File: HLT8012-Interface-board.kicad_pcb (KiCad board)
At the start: 2 copper layers, 33 x 32.5 mm, 18 parts, among them J1 +(ev), J2 -(ev), J3 LOAD, J4 DC, U1 HLW8012

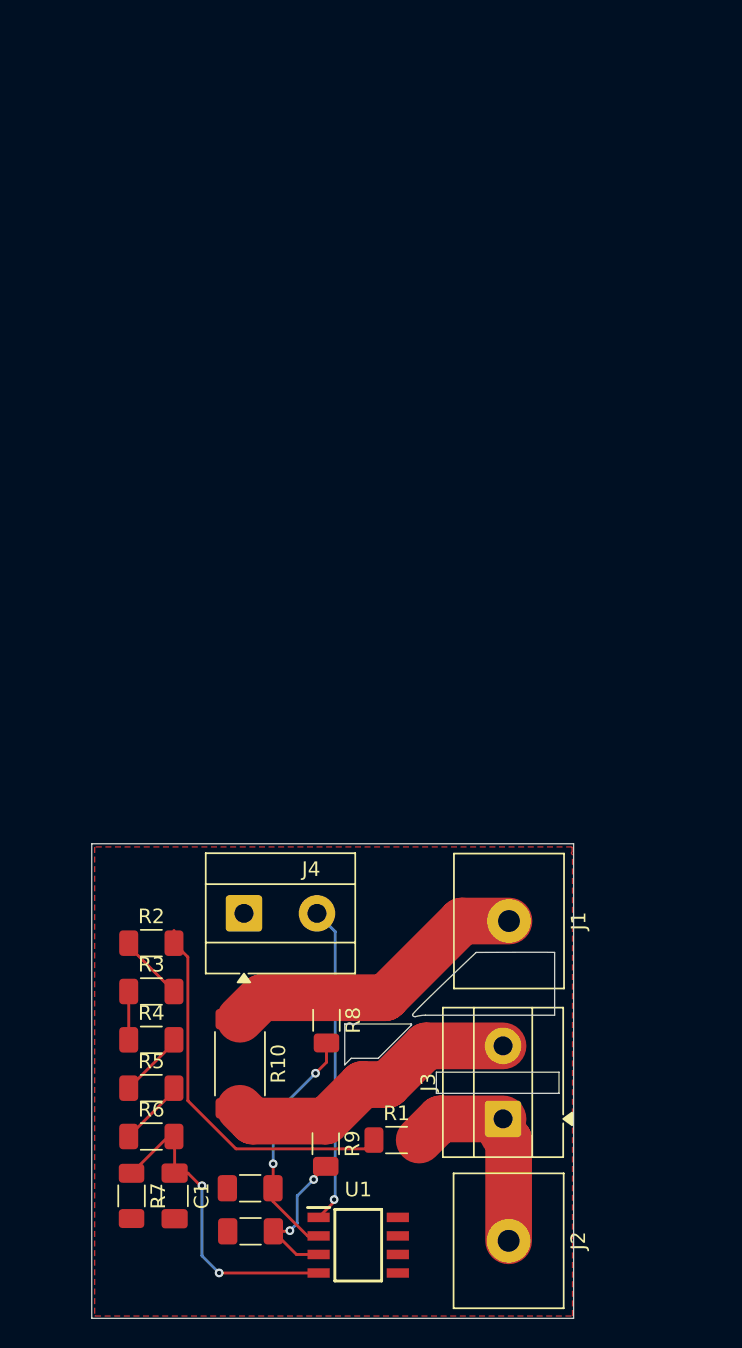
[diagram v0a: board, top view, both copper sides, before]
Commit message: ESP01 fix
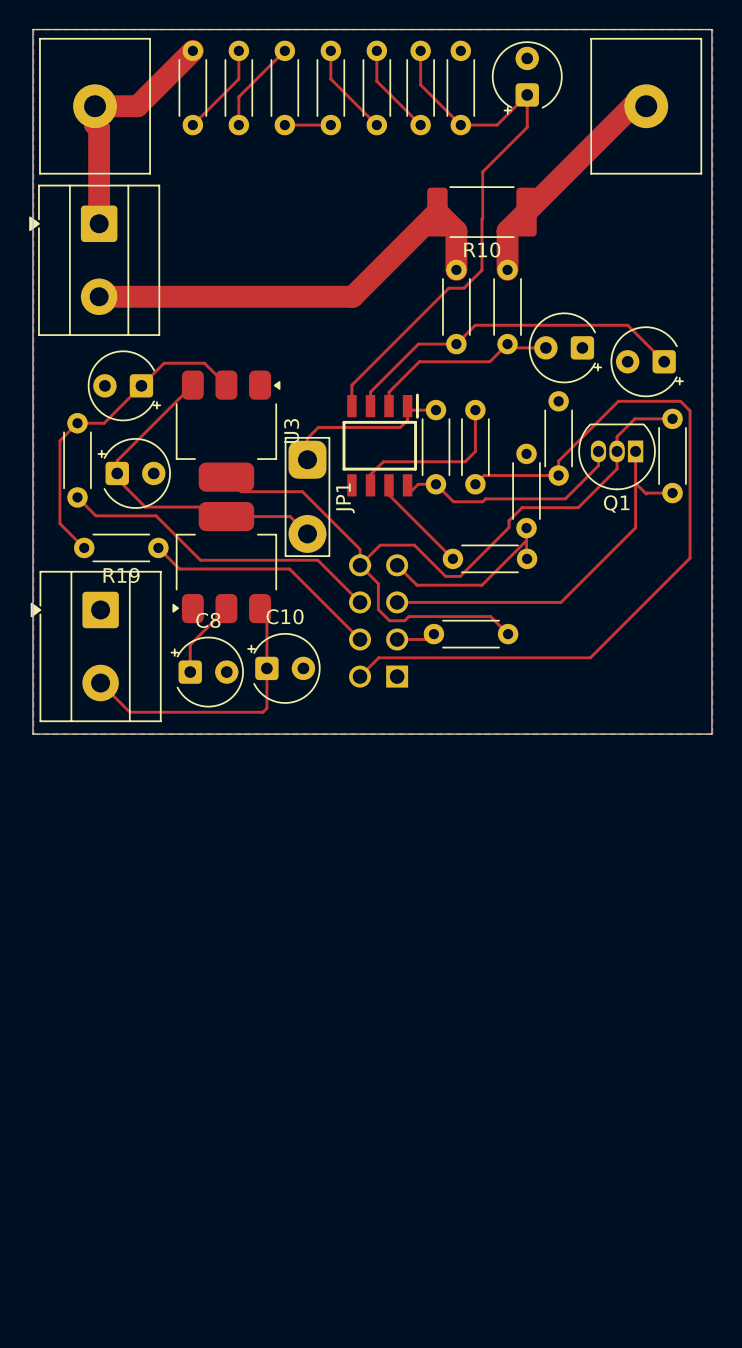
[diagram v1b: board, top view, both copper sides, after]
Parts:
- added C10: 22uF, Capacitor_THT:CP_Radial_Tantal_D4.5mm_P2.50mm, F.Cu at (122.2, 92.8)
- added C4: 22uF, Capacitor_THT:CP_Radial_Tantal_D4.5mm_P2.50mm, F.Cu at (112.0, 79.4)
- added C6: 100uF, Capacitor_THT:CP_Radial_Tantal_D4.5mm_P2.50mm, F.Cu at (113.6, 73.4)
- added C8: 100uF, Capacitor_THT:CP_Radial_Tantal_D4.5mm_P2.50mm, F.Cu at (117.0, 93.0)
- added JP1: Jumper_2_Bridged, TestPoint:TestPoint_2Pads_Pitch5.08mm_Drill1.3mm, F.Cu at (125.0, 78.5)
- added Q1: 2N7000, Package_TO_SOT_THT:TO-92_Inline, F.Cu at (147.5, 77.9)
- added R11: 470K, Resistor_THT:R_Axial_DIN0204_L3.6mm_D1.6mm_P5.08mm_Horizontal, F.Cu at (132.8, 55.5)
- added R12: 10K, Resistor_THT:R_Axial_DIN0204_L3.6mm_D1.6mm_P5.08mm_Horizontal, F.Cu at (133.8, 80.1)
- added R13: 10K, Resistor_THT:R_Axial_DIN0204_L3.6mm_D1.6mm_P5.08mm_Horizontal, F.Cu at (135.0, 85.2)
- added R14: 15K, Resistor_THT:R_Axial_DIN0204_L3.6mm_D1.6mm_P5.08mm_Horizontal, F.Cu at (140.0, 83.1)
- added R15: 15K, Resistor_THT:R_Axial_DIN0204_L3.6mm_D1.6mm_P5.08mm_Horizontal, F.Cu at (142.2, 74.5)
- added R16: 10K, Resistor_THT:R_Axial_DIN0204_L3.6mm_D1.6mm_P5.08mm_Horizontal, F.Cu at (136.5, 80.1)
- added R17: 10K, Resistor_THT:R_Axial_DIN0204_L3.6mm_D1.6mm_P5.08mm_Horizontal, F.Cu at (109.2, 81.0)
- added R18: 10K, Resistor_THT:R_Axial_DIN0204_L3.6mm_D1.6mm_P5.08mm_Horizontal, F.Cu at (138.7, 90.4)
- added R19: 10K, Resistor_THT:R_Axial_DIN0204_L3.6mm_D1.6mm_P5.08mm_Horizontal, F.Cu at (114.8, 84.5)
- added U2: ESP-01, ESP-01:MODULE_ESP-01, B.Cu at (139.5, 89.5)
- added U3: AMS1117-3.3, Package_TO_SOT_SMD:SOT-223-3_TabPin2, F.Cu at (119.5, 76.5)
- added U4: AMS1117-5.0, Package_TO_SOT_SMD:SOT-223-3_TabPin2, F.Cu at (119.5, 85.5)
- C1, C2, C3: footprint Capacitor_SMD:C_1206_3216Metric_Pad1.33x1.80mm_HandSolder -> Capacitor_THT:CP_Radial_Tantal_D4.5mm_P2.50mm
- R1, R2, R3, R4, R5, R8, R9: footprint Resistor_SMD:R_1206_3216Metric_Pad1.30x1.75mm_HandSolder -> Resistor_THT:R_Axial_DIN0204_L3.6mm_D1.6mm_P5.08mm_Horizontal
- R6: value 470K -> 10K; footprint Resistor_SMD:R_1206_3216Metric_Pad1.30x1.75mm_HandSolder -> Resistor_THT:R_Axial_DIN0204_L3.6mm_D1.6mm_P5.08mm_Horizontal
- R7: value 470K -> 1K; footprint Resistor_SMD:R_1206_3216Metric_Pad1.30x1.75mm_HandSolder -> Resistor_THT:R_Axial_DIN0204_L3.6mm_D1.6mm_P5.08mm_Horizontal
- moved J2 82.7 mm to (110.5, 54.2)
- moved C1 79.2 mm to (140.1, 53.5), turned to 90 degrees
- moved R7 76.7 mm to (135.5, 55.5), turned to 90 degrees
- moved R1 70.9 mm to (117.2, 55.5), turned to 90 degrees
- moved R5 67.7 mm to (129.8, 55.5), turned to 90 degrees
- moved J3 67.3 mm to (110.7, 62.3), turned to -90 degrees
- moved C3 65.9 mm to (149.4, 71.8)
- moved R4 63.8 mm to (126.6, 55.5), turned to 90 degrees
- moved C2 61.9 mm to (143.8, 70.8), turned to 180 degrees
- moved R10 60.6 mm to (136.9, 61.5), turned to 180 degrees
- moved R9 60.5 mm to (135.2, 65.5)
- moved R3 60.0 mm to (123.5, 55.5), turned to 90 degrees
- moved R6 56.7 mm to (150.0, 80.7), turned to 90 degrees
- moved J1 56.6 mm to (148.2, 54.2)
- moved R2 56.3 mm to (120.3, 55.5), turned to 90 degrees
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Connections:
- J4 pad 2: +5V -> +12V
- R5 pad 2: Net-(R5-Pad2) -> Net-(R11-Pad1)
- R6 pad 1: Net-(R5-Pad2) -> SEL
- R6 pad 2: V2P -> +3.3V
- U1 pad 1: +5V -> Net-(JP1-A)
- U1 pad 6: CF -> Net-(U1-CF)
- U1 pad 7: CF1 -> Net-(U1-CF1)
- U1 pad 8: SEL -> Net-(Q1-D)
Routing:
- net +3.3V: track 0.00 -> 78.4 mm
- net CF: track 0.00 -> 54.2 mm
- net SEL: track 0.00 -> 26.5 mm
- net Net-(U2-~{RST}): track 0.00 -> 22.3 mm
- net Net-(R1-Pad1): track 26.4 -> 6.38 mm
- net +12V: track 0.00 -> 19.4 mm
- net Net-(U2-CH_PD): track 0.00 -> 16.4 mm
- net V2P: track 22.6 -> 38.5 mm, vias 2 -> 0
- net Net-(Q1-D): track 0.00 -> 15.9 mm
- net Net-(U1-V1N): track 10.5 -> 24.2 mm, vias 2 -> 0
- net CF1: track 0.00 -> 12.8 mm
- net Net-(JP1-A): track 0.00 -> 11.9 mm
- net Net-(U1-CF): track 0.00 -> 11.4 mm
- net /LOAD: track 20.5 -> 30.1 mm
- net +5V: track 21.8 -> 29.2 mm, vias 1 -> 0
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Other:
- board size 33 x 32.5 mm -> 46.5 x 48.2 mm

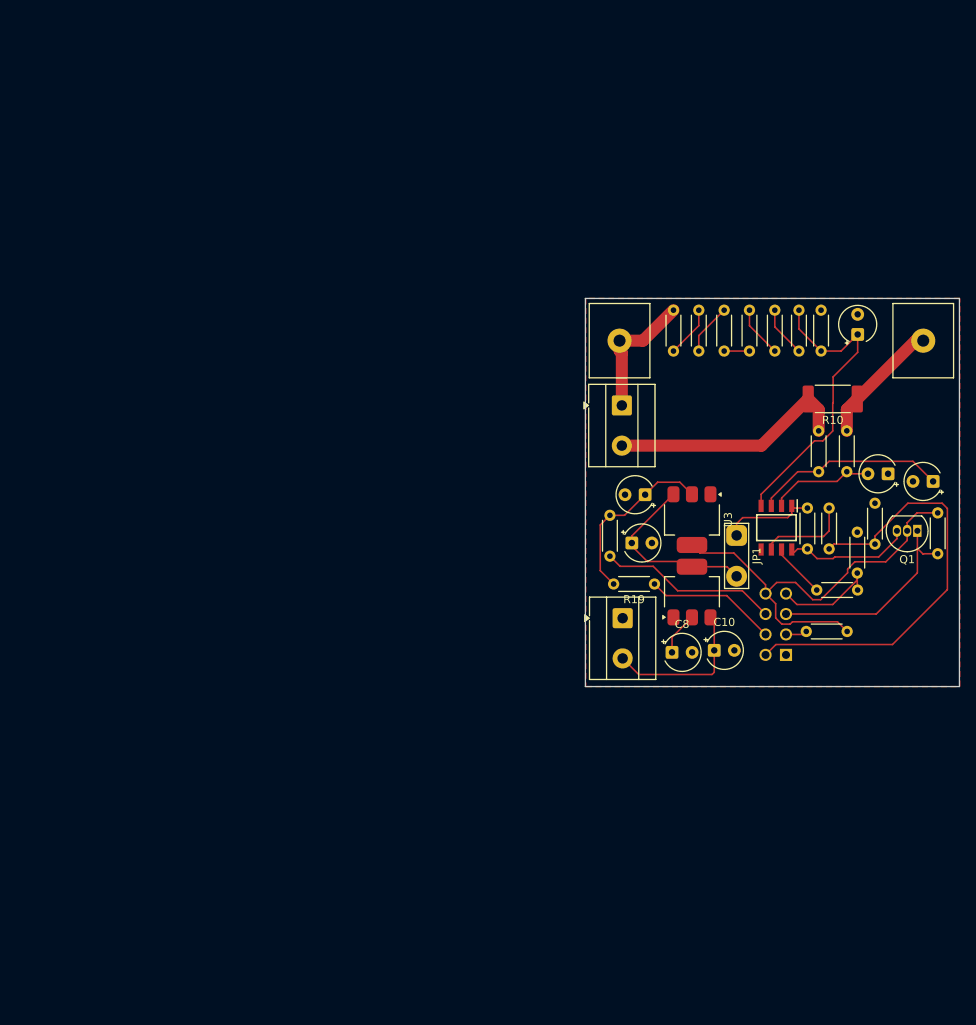
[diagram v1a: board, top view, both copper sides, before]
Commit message: Power module with LNK302
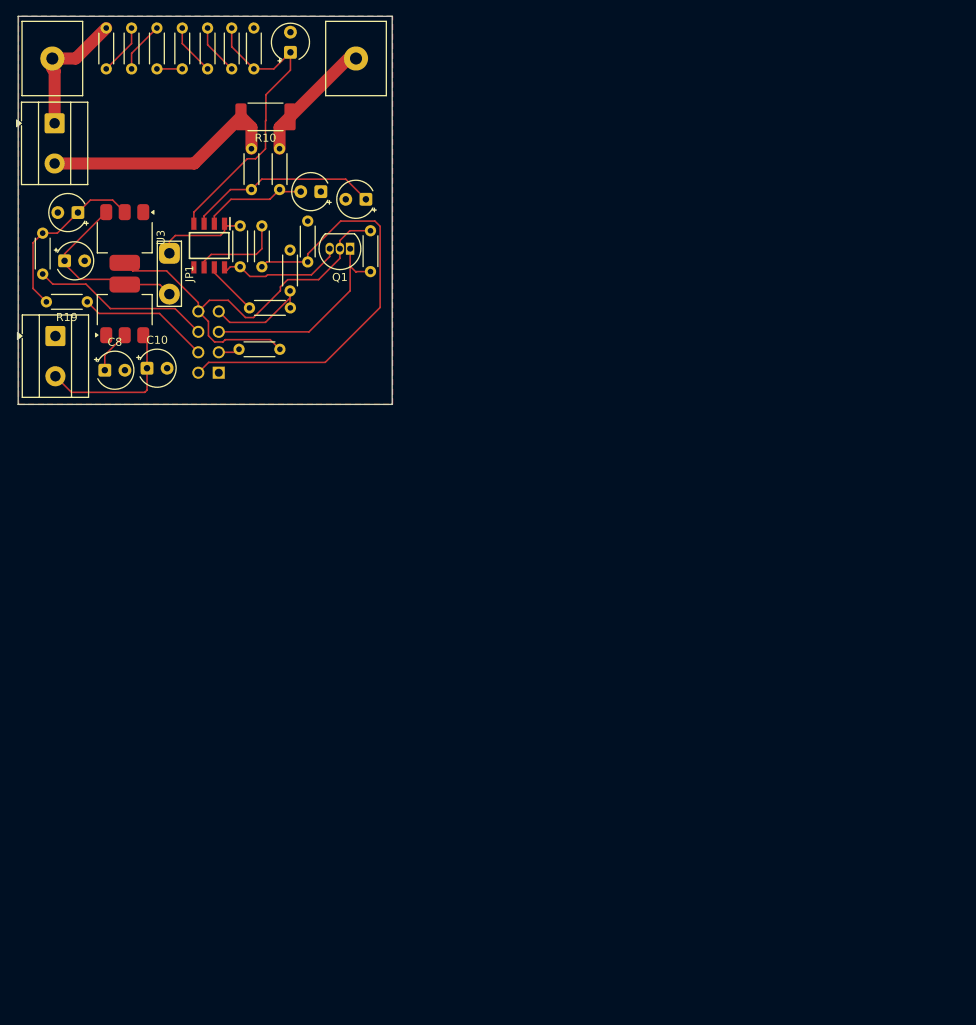
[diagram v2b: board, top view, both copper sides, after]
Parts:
- moved C1 78.8 mm to (69.5, 18.4)
- moved R1 78.8 mm to (46.6, 20.5)
- moved R12 78.8 mm to (63.3, 45.1)
- moved R18 78.8 mm to (68.2, 55.3)
- moved C2 78.8 mm to (73.3, 35.7)
- moved C3 78.8 mm to (78.9, 36.7)
- moved C6 78.8 mm to (43.1, 38.3)
- moved J2 78.8 mm to (39.9, 19.2)
- moved J3 78.8 mm to (40.2, 27.2)
- moved JP1 78.8 mm to (54.5, 43.4)
- moved Q1 78.8 mm to (77.0, 42.8)
- moved R11 78.8 mm to (62.2, 20.5)
- moved R13 78.8 mm to (64.4, 50.2)
- moved R14 78.8 mm to (69.5, 48.1)
- moved R16 78.8 mm to (66.0, 45.1)
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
